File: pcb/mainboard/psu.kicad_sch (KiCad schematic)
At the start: 133 parts, among them J1 CONN_PCIE_PWR_8PIN, J2 CONN_IBC_MGMT, J3 CONN_01X03, J4 CONN_01X05, SW1 SWITCH, SW2 SWITCH, U1 STM32L031C6U6, U2 MYMGK1R812ERSR, U26 LMR70503, U3 MYMGK00504ERSR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

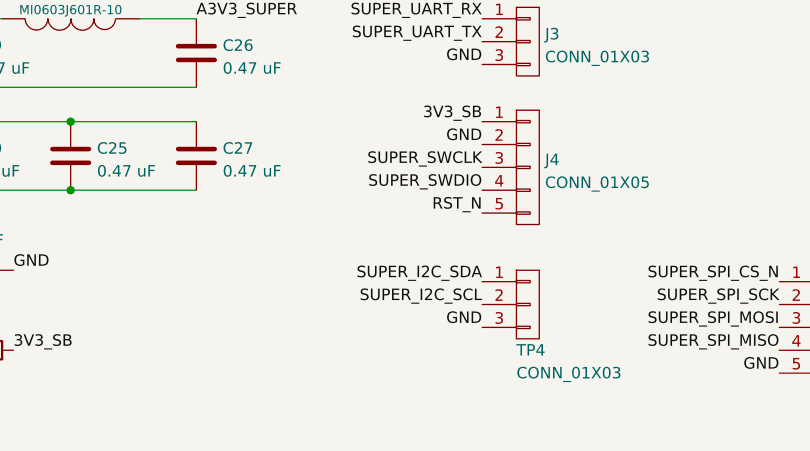
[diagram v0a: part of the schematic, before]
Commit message: Tweaks to debug connectors, hooked up TX DAC
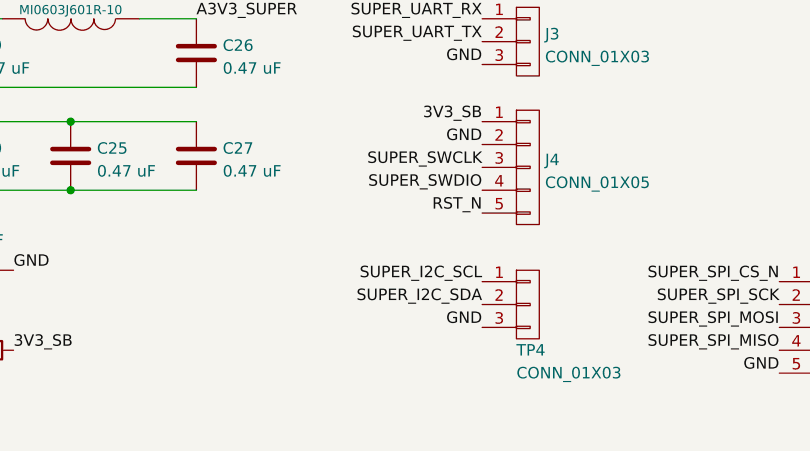
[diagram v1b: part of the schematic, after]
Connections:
- net SUPER_I2C_SCL: now also TP4.1 (P1); no longer TP4.2 (P2)
- net SUPER_I2C_SDA: now also TP4.2 (P2); no longer TP4.1 (P1)
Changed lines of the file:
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@@
     (effects (font (size 1.27 1.27)) (justify right bottom))
   )
-  (label "SUPER_I2C_SCL" (at 276.86 387.35 180)
+  (label "SUPER_I2C_SCL" (at 276.86 384.81 180)
     (effects (font (size 1.27 1.27)) (justify right bottom))
   )
@@
     (effects (font (size 1.27 1.27)) (justify right bottom))
   )
-  (label "SUPER_I2C_SDA" (at 276.86 384.81 180)
-    (effects (font (size 1.27 1.27)) (justify right bottom))
-  )
+  (label "SUPER_I2C_SDA" (at 276.86 387.35 180)
+    (effects (font (size 1.27 1.27)) (justify right bottom))
+  )

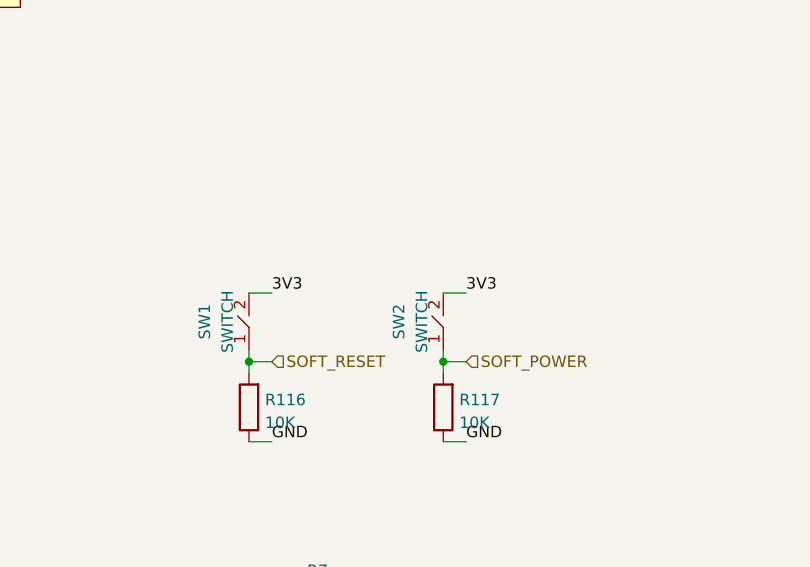
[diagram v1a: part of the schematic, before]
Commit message: Hooked up soft power/reset buttons
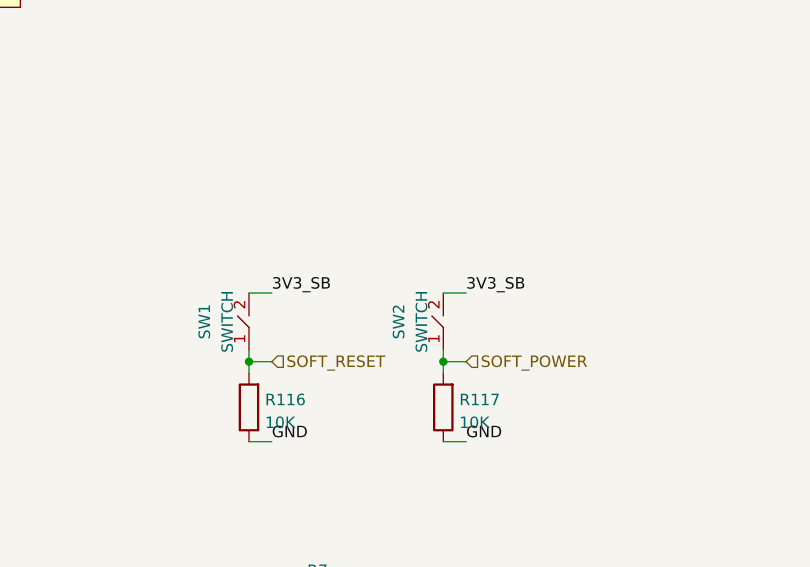
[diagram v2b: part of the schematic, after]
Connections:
- net 3V3: no longer SW1.2, SW2.2
- net 3V3_SB: now also SW1.2, SW2.2
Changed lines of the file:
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@@
     (effects (font (size 1.27 1.27)) (justify right bottom))
   )
-  (label "3V3" (at 109.22 314.96 0)
+  (label "3V3_SB" (at 109.22 314.96 0)
     (effects (font (size 1.27 1.27)) (justify left bottom))
   )
@@
     (effects (font (size 1.27 1.27)) (justify right bottom))
   )
-  (label "3V3" (at 130.81 314.96 0)
+  (label "3V3_SB" (at 130.81 314.96 0)
     (effects (font (size 1.27 1.27)) (justify left bottom))
   )

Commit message: More work in supervisor region
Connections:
- net 12V0_VMON: now also U1.19 (PB1); no longer U1.11 (PA1)
- net 1V2_EN: now also U1.13 (PA3); no longer U1.19 (PB1)
- net FPGA_INIT: now also U1.11 (PA1); no longer U1.13 (PA3)
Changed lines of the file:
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@@
     (effects (font (size 1.27 1.27)) (justify right bottom))
   )
-  (label "1V2_EN" (at 78.74 353.06 180)
+  (label "1V2_EN" (at 35.56 358.14 180)
     (effects (font (size 1.27 1.27)) (justify right bottom))
   )
@@
     (effects (font (size 1.27 1.27)) (justify right bottom))
   )
-  (label "12V0_VMON" (at 35.56 353.06 180)
+  (label "12V0_VMON" (at 78.74 353.06 180)
     (effects (font (size 1.27 1.27)) (justify right bottom))
   )
@@
     (effects (font (size 1.27 1.27)) (justify right))
   )
-  (hierarchical_label "FPGA_INIT" (shape bidirectional) (at 35.56 358.14 180)
+  (hierarchical_label "FPGA_INIT" (shape bidirectional) (at 35.56 353.06 180)
     (effects (font (size 1.27 1.27)) (justify right))
   )
@@
     )
     (pin "10")
-    (pin "11" (alternate "ADC_IN1"))
+    (pin "11")
     (pin "12")
     (pin "13")
@@
     (pin "15" (alternate "SPI1_SCK"))
     (pin "16" (alternate "SPI1_MISO"))
-    (pin "17" (alternate "SPI1_MOSI"))
+    (pin "17")
     (pin "29")
     (pin "30" (alternate "I2C1_SCL"))
@@
     (pin "38")
     (pin "18")
-    (pin "19")
+    (pin "19" (alternate "ADC_IN9"))
     (pin "20")
     (pin "21")
@@
     )
     (pin "10")
-    (pin "11" (alternate "ADC_IN1"))
+    (pin "11")
     (pin "12")
     (pin "13")
@@
     (pin "15" (alternate "SPI1_SCK"))
     (pin "16" (alternate "SPI1_MISO"))
-    (pin "17" (alternate "SPI1_MOSI"))
+    (pin "17")
     (pin "29")
     (pin "30" (alternate "I2C1_SCL"))
@@
     (pin "38")
     (pin "18")
-    (pin "19")
+    (pin "19" (alternate "ADC_IN9"))
     (pin "20")
     (pin "21")
@@
     )
     (pin "10")
-    (pin "11" (alternate "ADC_IN1"))
+    (pin "11")
     (pin "12")
     (pin "13")
@@
     (pin "15" (alternate "SPI1_SCK"))
     (pin "16" (alternate "SPI1_MISO"))
-    (pin "17" (alternate "SPI1_MOSI"))
+    (pin "17")
     (pin "29")
     (pin "30" (alternate "I2C1_SCL"))
@@
     (pin "38")
     (pin "18")
-    (pin "19")
+    (pin "19" (alternate "ADC_IN9"))
     (pin "20")
     (pin "21")
@@
     )
     (pin "10")
-    (pin "11" (alternate "ADC_IN1"))
+    (pin "11")
     (pin "12")
     (pin "13")
@@
     (pin "15" (alternate "SPI1_SCK"))
     (pin "16" (alternate "SPI1_MISO"))
-    (pin "17" (alternate "SPI1_MOSI"))
+    (pin "17")
     (pin "29")
     (pin "30" (alternate "I2C1_SCL"))
@@
     (pin "38")
     (pin "18")
-    (pin "19")
+    (pin "19" (alternate "ADC_IN9"))
     (pin "20")
     (pin "21")
@@
     )
     (pin "10")
-    (pin "11" (alternate "ADC_IN1"))
+    (pin "11")
     (pin "12")
     (pin "13")
@@
     (pin "15" (alternate "SPI1_SCK"))
     (pin "16" (alternate "SPI1_MISO"))
-    (pin "17" (alternate "SPI1_MOSI"))
+    (pin "17")
     (pin "29")
     (pin "30" (alternate "I2C1_SCL"))
@@
     (pin "38")
     (pin "18")
-    (pin "19")
+    (pin "19" (alternate "ADC_IN9"))
     (pin "20")
     (pin "21")

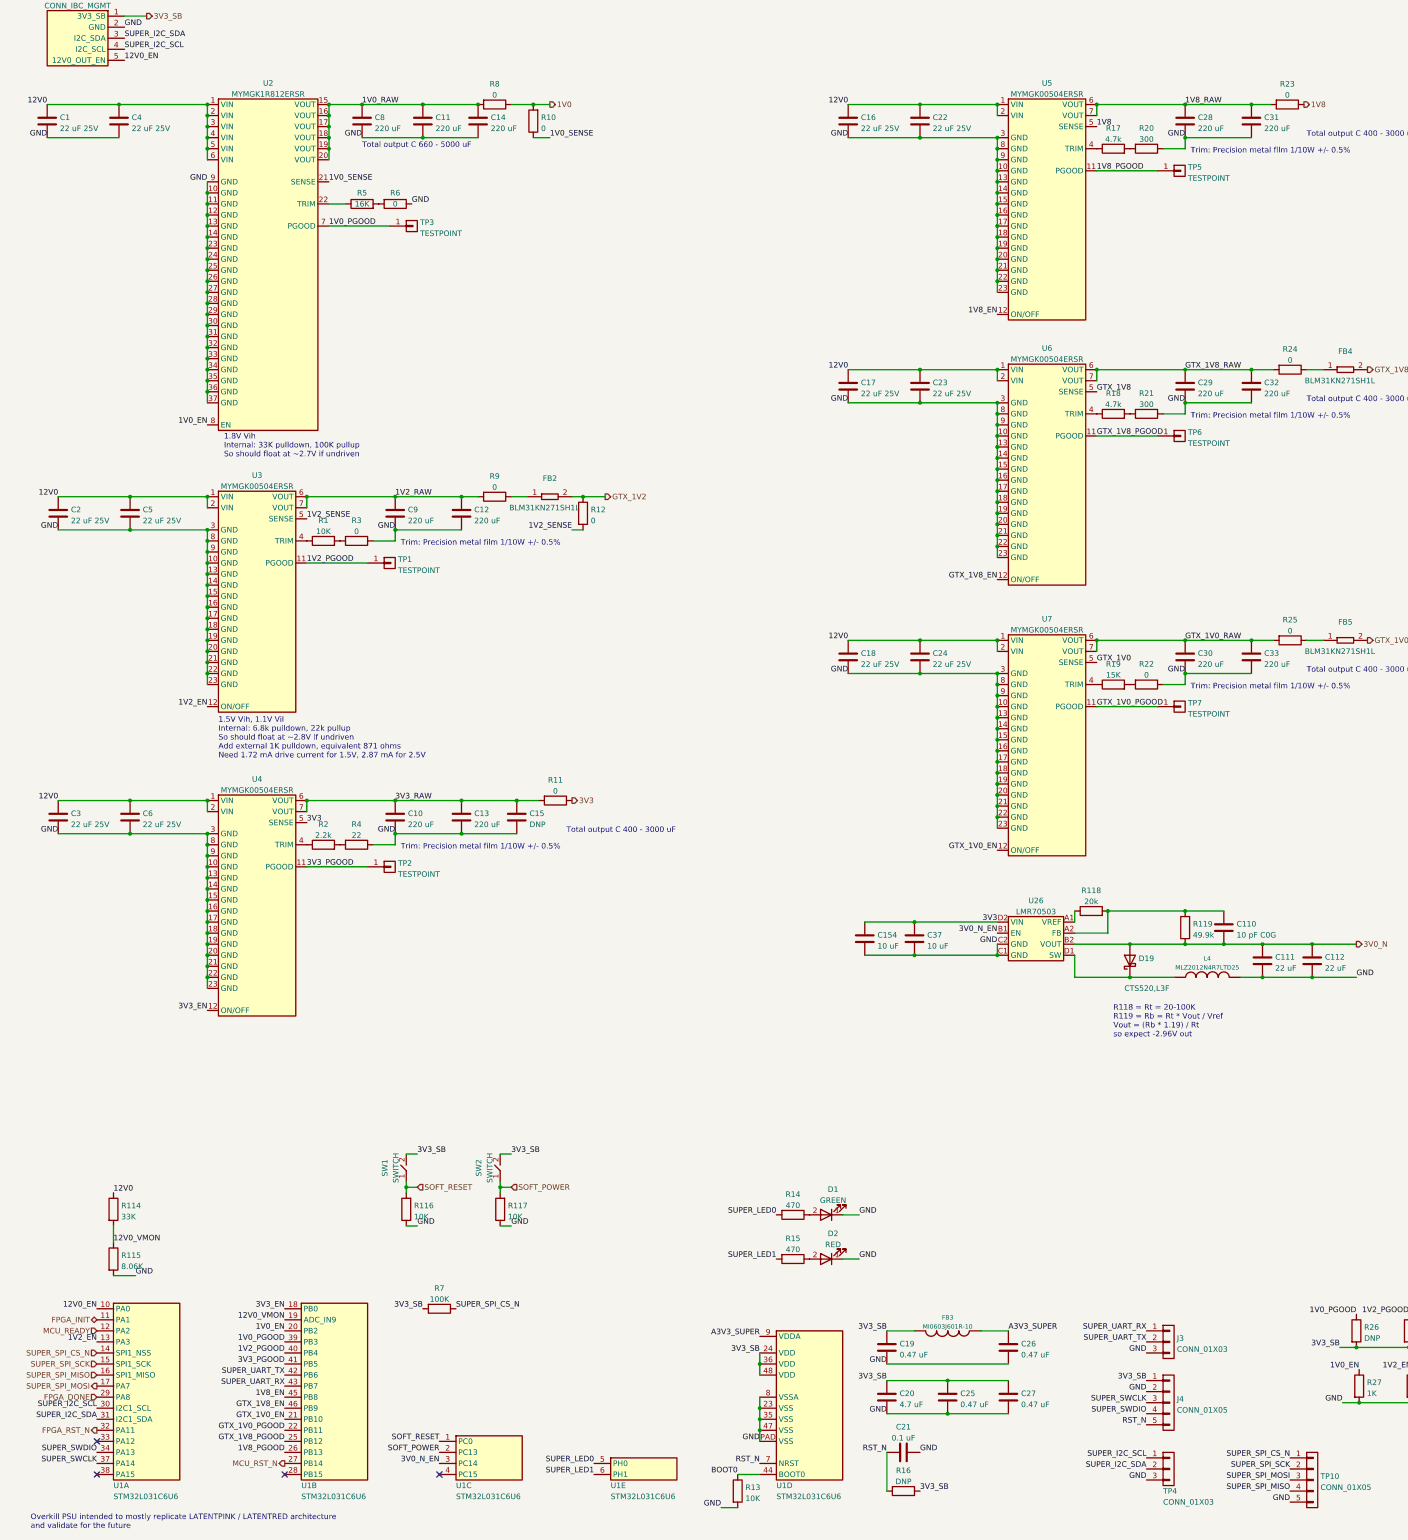
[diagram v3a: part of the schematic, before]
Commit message: Continued layout, started plane fills. Everything routed except 1V8 regulator
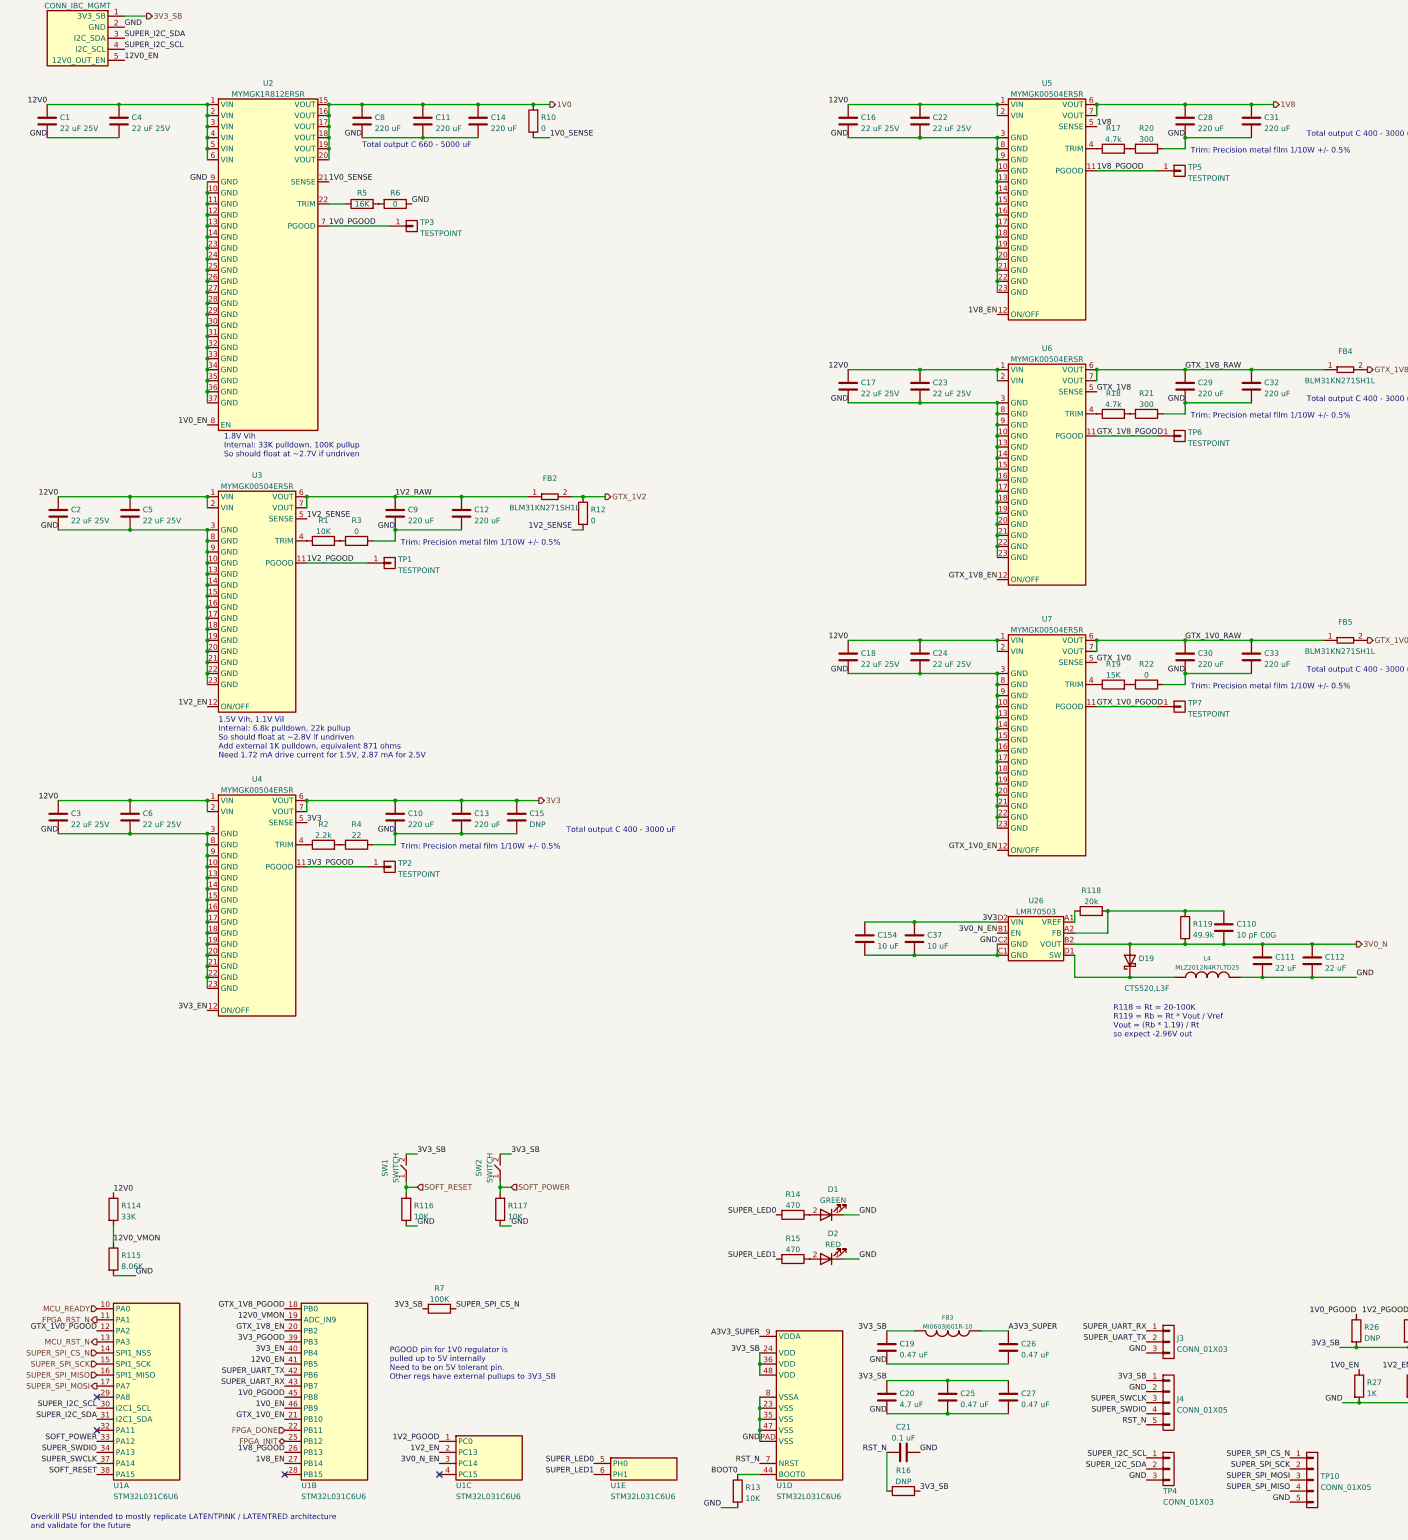
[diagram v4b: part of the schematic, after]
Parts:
- removed R11, R23, R24, R25, R8, R9: 0, azonenberg_pcb:EIA_0402_RES_NOSILK, symbol passive-azonenberg:R_PWR
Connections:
- net 1V0_RAW is gone; now on net 1V0: C11.1, C14.1, C8.1, U2.15 (VOUT), U2.16 (VOUT), U2.17 (VOUT), U2.18 (VOUT), U2.19 (VOUT), U2.20 (VOUT)
- net 1V8_RAW is gone; now on net 1V8: C28.1, C31.1, U5.6 (VOUT), U5.7 (VOUT)
- net 3V3_RAW is gone; now on net 3V3: C10.1, C13.1, C15.1, U4.6 (VOUT), U4.7 (VOUT)
- net 12V0_EN: now also U1.41 (PB5); no longer U1.10 (PA0)
- net 1V0_EN: now also U1.46 (PB9); no longer U1.20 (PB2)
- net 1V0_PGOOD: now also U1.45 (PB8); no longer U1.39 (PB3)
- net 1V2_EN: now also U1.2 (PC13); no longer U1.13 (PA3)
- net 1V2_PGOOD: now also U1.1 (PC0); no longer U1.40 (PB4)
- net 1V2_RAW: now also FB2.1
- net 1V8_EN: now also U1.27 (PB14); no longer U1.45 (PB8)
- net 3V3_EN: now also U1.40 (PB4); no longer U1.18 (PB0)
- net 3V3_PGOOD: now also U1.39 (PB3); no longer U1.41 (PB5)
- net FPGA_DONE: now also U1.22 (PB11); no longer U1.29 (PA8)
- net FPGA_INIT: now also U1.25 (PB12); no longer U1.11 (PA1)
- net FPGA_RST_N: now also U1.11 (PA1); no longer U1.32 (PA11)
- net GTX_1V0_PGOOD: now also U1.12 (PA2); no longer U1.22 (PB11)
- net GTX_1V0_RAW: now also FB5.1
- net GTX_1V8_EN: now also U1.20 (PB2); no longer U1.46 (PB9)
- net GTX_1V8_PGOOD: now also U1.18 (PB0); no longer U1.25 (PB12)
- net GTX_1V8_RAW: now also FB4.1
- net MCU_READY: now also U1.10 (PA0); no longer U1.12 (PA2)
- net MCU_RST_N: now also U1.13 (PA3); no longer U1.27 (PB14)
- net SOFT_POWER: now also U1.33 (PA12); no longer U1.2 (PC13)
- net SOFT_RESET: now also U1.38 (PA15); no longer U1.1 (PC0)
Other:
- note added: "PGOOD pin for 1V0 regulator is pulled up to 5V internally Need to be on 5V tolerant pin. Other regs have external pullups to 3V3_SB"
